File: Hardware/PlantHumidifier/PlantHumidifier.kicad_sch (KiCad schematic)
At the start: 10 parts

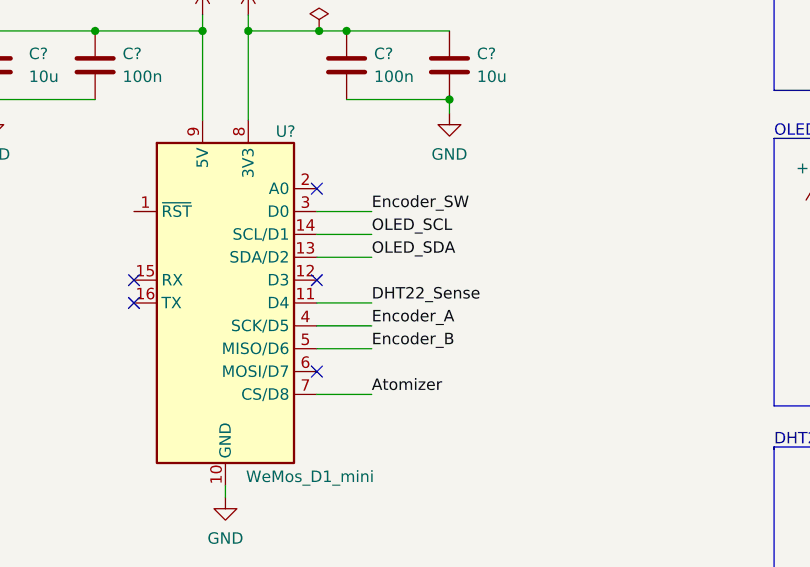
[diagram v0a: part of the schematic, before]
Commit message: Move DHT22 pin in code and schematic to D3 (GPIO 0); GPIO requires removal of DHT b/w resets
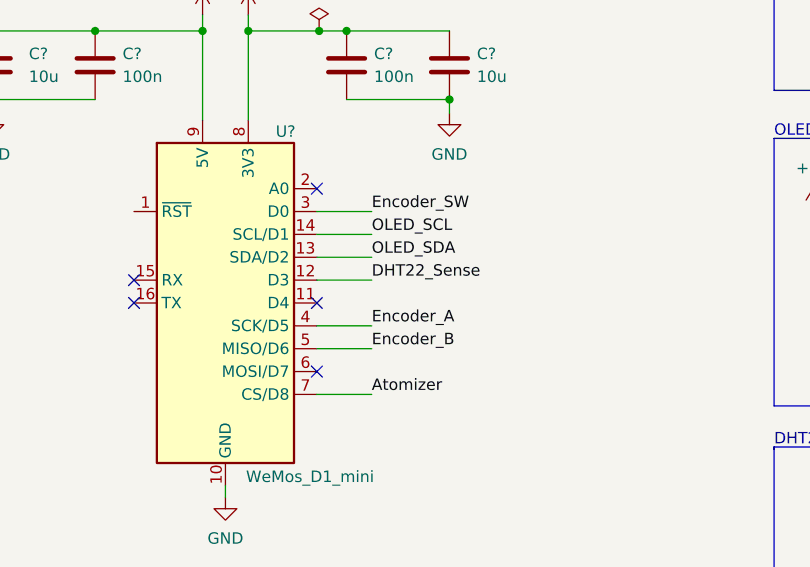
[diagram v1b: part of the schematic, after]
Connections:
- net DHT22_Sense: now also U?.12 (D3); no longer U?.11 (D4)
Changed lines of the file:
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@@
   (no_connect (at 125.476 116.078))
   (no_connect (at 105.156 105.918))
-  (no_connect (at 125.476 105.918))
+  (no_connect (at 125.476 108.458))
   (no_connect (at 105.156 108.458))
   (no_connect (at 125.476 95.758))
@@
     (stroke (width 0) (type default) (color 0 0 0 0))
   )
-  (wire (pts (xy 125.476 108.458) (xy 131.572 108.458))
+  (wire (pts (xy 125.476 105.918) (xy 131.572 105.918))
     (stroke (width 0) (type default) (color 0 0 0 0))
   )
@@
     (effects (font (size 1.27 1.27)) (justify left bottom))
   )
-  (label "DHT22_Sense" (at 131.572 108.458 0)
-    (effects (font (size 1.27 1.27)) (justify left bottom))
-  )
+  (label "DHT22_Sense" (at 131.572 105.918 0)
+    (effects (font (size 1.27 1.27)) (justify left bottom))
+  )

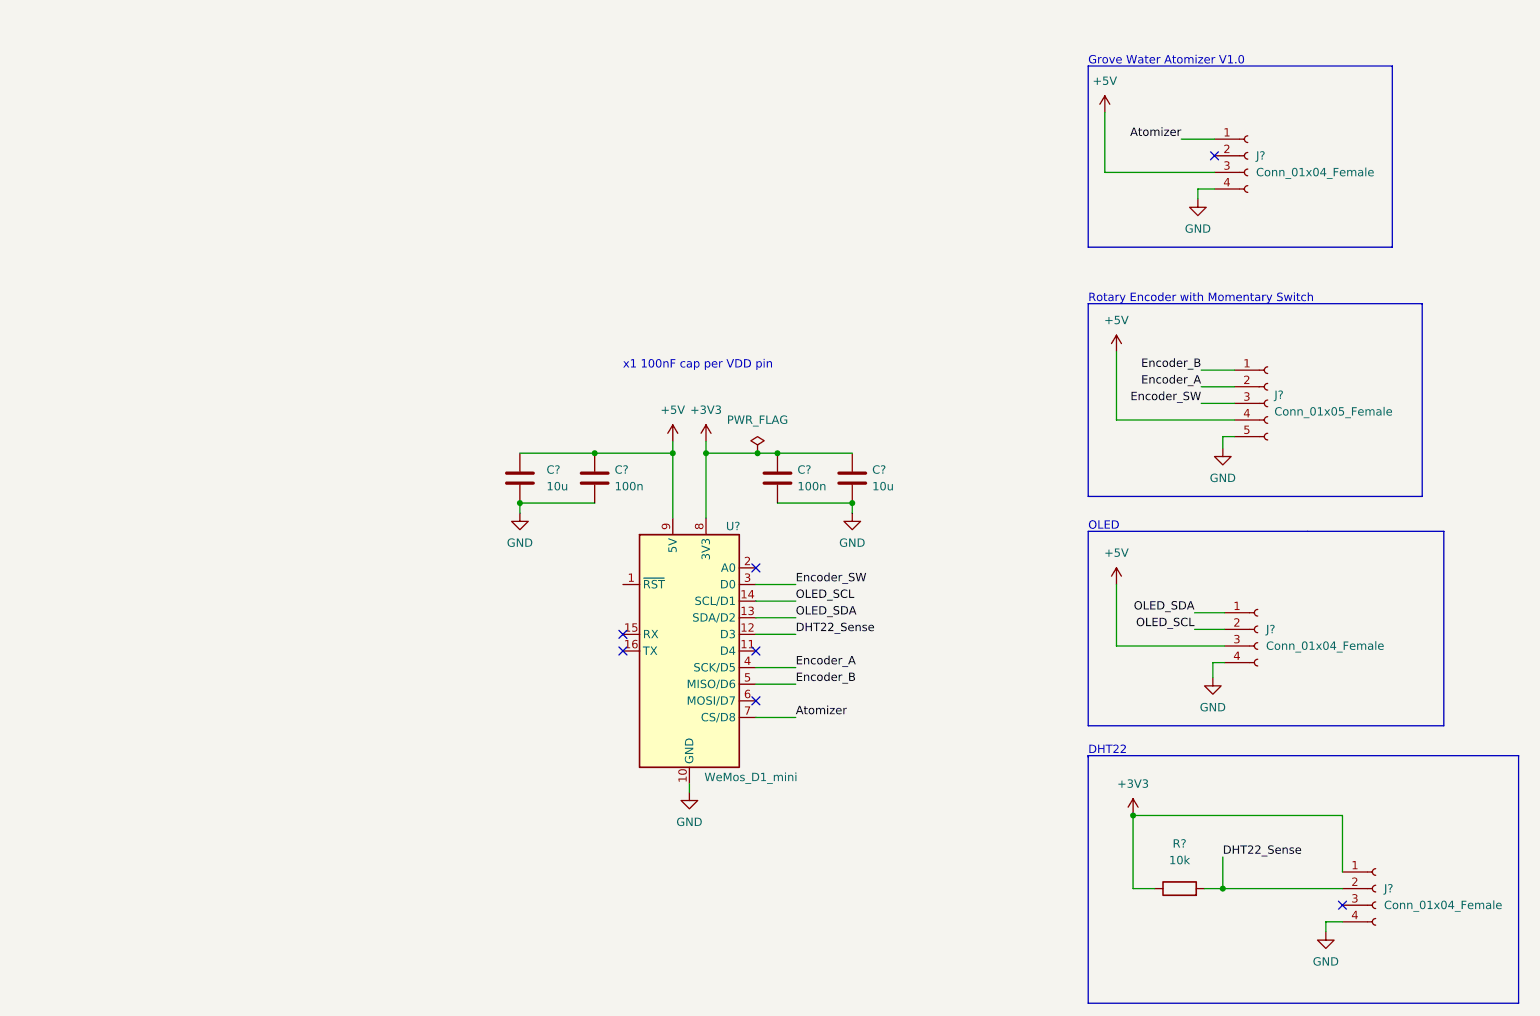
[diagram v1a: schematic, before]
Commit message: Schematic: Add an active low reset switch
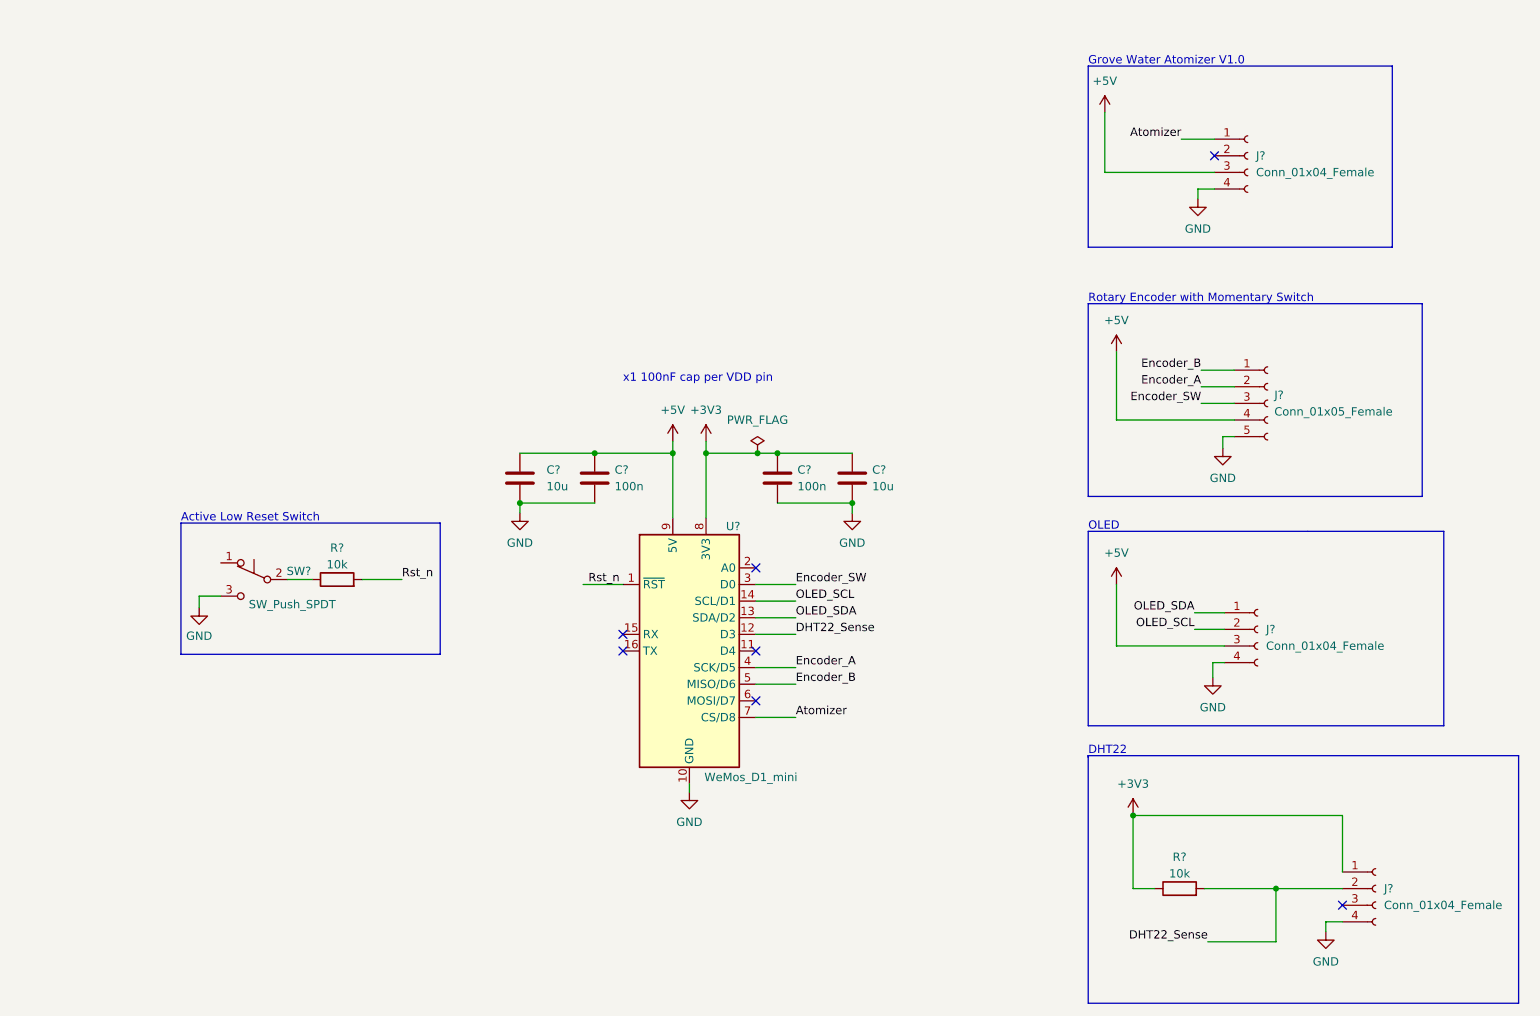
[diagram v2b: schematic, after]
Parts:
- added R?: 10k, symbol Device:R
- added SW?: SW_Push_SPDT, symbol Switch:SW_Push_SPDT
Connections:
- net GND: now also SW?.3 (C)
- net Rst_n: now reaches U?.1 (~{RST})
- net Rst_n: now also R?.2
- new net: R?.1, SW?.2 (B)
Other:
- note added: "Active Low Reset Switch"
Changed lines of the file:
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@@
   (junction (at 125.73 78.232) (diameter 0) (color 0 0 0 0)
   )
-  (junction (at 196.85 144.78) (diameter 0) (color 0 0 0 0)
-  )
   (junction (at 100.838 78.232) (diameter 0) (color 0 0 0 0)
   )
@@
   )
   (junction (at 112.776 78.232) (diameter 0) (color 0 0 0 0)
+  )
+  (junction (at 204.978 144.78) (diameter 0) (color 0 0 0 0)
   )
   (junction (at 128.778 78.232) (diameter 0) (color 0 0 0 0)
@@
     (stroke (width 0) (type default) (color 0 0 0 0))
   )
+  (polyline (pts (xy 77.216 108.966) (xy 37.592 108.966))
+    (stroke (width 0) (type default) (color 0 0 0 0))
+  )
   (wire (pts (xy 125.476 98.298) (xy 131.572 98.298))
     (stroke (width 0) (type default) (color 0 0 0 0))
@@
     (stroke (width 0) (type default) (color 0 0 0 0))
   )
+  (polyline (pts (xy 77.216 88.9) (xy 77.216 108.966))
+    (stroke (width 0) (type default) (color 0 0 0 0))
+  )
   (polyline (pts (xy 176.276 19.05) (xy 176.276 46.736))
     (stroke (width 0) (type default) (color 0 0 0 0))
@@
     (stroke (width 0) (type default) (color 0 0 0 0))
   )
-  (wire (pts (xy 196.85 144.78) (xy 215.138 144.78))
+  (polyline (pts (xy 37.592 88.9) (xy 77.216 88.9))
+    (stroke (width 0) (type default) (color 0 0 0 0))
+  )
+  (wire (pts (xy 194.056 144.78) (xy 204.978 144.78))
     (stroke (width 0) (type default) (color 0 0 0 0))
   )
@@
     (stroke (width 0) (type default) (color 0 0 0 0))
   )
+  (wire (pts (xy 204.978 144.78) (xy 204.978 152.908))
+    (stroke (width 0) (type default) (color 0 0 0 0))
+  )
   (polyline (pts (xy 222.758 46.736) (xy 222.758 19.05))
     (stroke (width 0) (type default) (color 0 0 0 0))
   )
+  (wire (pts (xy 194.564 152.908) (xy 204.978 152.908))
+    (stroke (width 0) (type default) (color 0 0 0 0))
+  )
   (wire (pts (xy 112.776 78.232) (xy 112.776 88.138))
     (stroke (width 0) (type default) (color 0 0 0 0))
@@
     (stroke (width 0) (type default) (color 0 0 0 0))
   )
-  (wire (pts (xy 194.056 144.78) (xy 196.85 144.78))
+  (wire (pts (xy 40.386 101.854) (xy 40.386 100.076))
     (stroke (width 0) (type default) (color 0 0 0 0))
   )
@@
     (stroke (width 0) (type default) (color 0 0 0 0))
   )
+  (wire (pts (xy 204.978 144.78) (xy 215.138 144.78))
+    (stroke (width 0) (type default) (color 0 0 0 0))
+  )
   (polyline (pts (xy 209.804 90.17) (xy 176.276 90.17))
     (stroke (width 0) (type default) (color 0 0 0 0))
@@
     (stroke (width 0) (type default) (color 0 0 0 0))
   )
+  (wire (pts (xy 40.386 100.076) (xy 43.688 100.076))
+    (stroke (width 0) (type default) (color 0 0 0 0))
+  )
   (wire (pts (xy 89.408 85.852) (xy 100.838 85.852))
     (stroke (width 0) (type default) (color 0 0 0 0))
   )
+  (wire (pts (xy 65.278 97.536) (xy 71.374 97.536))
+    (stroke (width 0) (type default) (color 0 0 0 0))
+  )
   (wire (pts (xy 128.778 78.232) (xy 140.208 78.232))
     (stroke (width 0) (type default) (color 0 0 0 0))
   )
+  (wire (pts (xy 53.848 97.536) (xy 57.658 97.536))
+    (stroke (width 0) (type default) (color 0 0 0 0))
+  )
   (polyline (pts (xy 176.276 119.888) (xy 230.632 119.888))
     (stroke (width 0) (type default) (color 0 0 0 0))
@@
     (stroke (width 0) (type default) (color 0 0 0 0))
   )
+  (polyline (pts (xy 37.592 108.966) (xy 37.592 88.9))
+    (stroke (width 0) (type default) (color 0 0 0 0))
+  )
   (wire (pts (xy 183.134 144.78) (xy 186.436 144.78))
     (stroke (width 0) (type default) (color 0 0 0 0))
   )
+  (wire (pts (xy 99.06 98.298) (xy 105.156 98.298))
+    (stroke (width 0) (type default) (color 0 0 0 0))
+  )
   (wire (pts (xy 196.85 77.47) (xy 196.85 75.692))
     (stroke (width 0) (type default) (color 0 0 0 0))
   )
-  (wire (pts (xy 196.85 139.954) (xy 196.85 144.78))
-    (stroke (width 0) (type default) (color 0 0 0 0))
-  )
   (polyline (pts (xy 176.276 55.372) (xy 176.276 84.836))
     (stroke (width 0) (type default) (color 0 0 0 0))
@@
     (stroke (width 0) (type default) (color 0 0 0 0))
   )
-  (text "x1 100nF cap per VDD pin" (at 105.156 65.532 0)
+  (text "x1 100nF cap per VDD pin" (at 105.156 67.564 0)
     (effects (font (size 1.27 1.27)) (justify left bottom))
   )
@@
     (effects (font (size 1.27 1.27)) (justify left bottom))
   )
+  (text "Active Low Reset Switch" (at 37.592 88.9 0)
+    (effects (font (size 1.27 1.27)) (justify left bottom))
+  )
   (label "OLED_SDA" (at 131.572 103.378 0)
     (effects (font (size 1.27 1.27)) (justify left bottom))
   )
   (label "DHT22_Sense" (at 131.572 105.918 0)
+    (effects (font (size 1.27 1.27)) (justify left bottom))
+  )
+  (label "Rst_n" (at 71.374 97.536 0)
     (effects (font (size 1.27 1.27)) (justify left bottom))
   )
@@
     (effects (font (size 1.27 1.27)) (justify right bottom))
   )
-  (label "DHT22_Sense" (at 196.85 139.954 0)
-    (effects (font (size 1.27 1.27)) (justify left bottom))
+  (label "Rst_n" (at 104.648 98.298 180)
+    (effects (font (size 1.27 1.27)) (justify right bottom))
+  )
+  (label "DHT22_Sense" (at 194.564 152.908 180)
+    (effects (font (size 1.27 1.27)) (justify right bottom))
   )
   (label "Atomizer" (at 190.5 30.226 180)
@@
     (pin "1")
   )
+  (symbol (lib_id "Switch:SW_Push_SPDT") (at 48.768 97.536 0) (mirror y) (unit 1)
+    (in_bom yes) (on_board yes)
+    (property "Reference" "SW?" (id 0) (at 55.626 96.266 0))
+    (property "Value" "SW_Push_SPDT" (id 1) (at 54.61 101.346 0))
+    (property "Footprint" "" (id 2) (at 48.768 97.536 0)
+      (effects (font (size 1.27 1.27)) hide)
+    )
+    (property "Datasheet" "~" (id 3) (at 48.768 97.536 0)
+      (effects (font (size 1.27 1.27)) hide)
+    )
+    (pin "1")
+    (pin "2")
+    (pin "3")
+  )
+  (symbol (lib_id "power:GND") (at 40.386 101.854 0) (unit 1)
+    (in_bom yes) (on_board yes)
+    (property "Reference" "#PWR?" (id 0) (at 40.386 108.204 0)
+      (effects (font (size 1.27 1.27)) hide)
+    )
+    (property "Value" "GND" (id 1) (at 40.386 106.172 0))
+    (property "Footprint" "" (id 2) (at 40.386 101.854 0)
+      (effects (font (size 1.27 1.27)) hide)
+    )
+    (property "Datasheet" "" (id 3) (at 40.386 101.854 0)
+      (effects (font (size 1.27 1.27)) hide)
+    )
+    (pin "1")
+  )
   (symbol (lib_id "Connector:Conn_01x04_Female") (at 202.184 105.156 0) (unit 1)
     (in_bom yes) (on_board yes) (fields_autoplaced)
@@
   )
   (symbol (lib_id "Device:R") (at 190.246 144.78 90) (unit 1)
-    (in_bom yes) (on_board yes) (fields_autoplaced)
-    (property "Reference" "R?" (id 0) (at 190.246 137.922 90))
-    (property "Value" "10k" (id 1) (at 190.246 140.462 90))
+    (in_bom yes) (on_board yes)
+    (property "Reference" "R?" (id 0) (at 190.246 139.954 90))
+    (property "Value" "10k" (id 1) (at 190.246 142.494 90))
     (property "Footprint" "" (id 2) (at 190.246 146.558 90)
       (effects (font (size 1.27 1.27)) hide)
@@
     )
     (property "Datasheet" "~" (id 3) (at 89.408 82.042 0)
+      (effects (font (size 1.27 1.27)) hide)
+    )
+    (pin "1")
+    (pin "2")
+  )
+  (symbol (lib_id "Device:R") (at 61.468 97.536 90) (unit 1)
+    (in_bom yes) (on_board yes)
+    (property "Reference" "R?" (id 0) (at 61.468 92.71 90))
+    (property "Value" "10k" (id 1) (at 61.468 95.25 90))
+    (property "Footprint" "" (id 2) (at 61.468 99.314 90)
+      (effects (font (size 1.27 1.27)) hide)
+    )
+    (property "Datasheet" "~" (id 3) (at 61.468 97.536 0)
       (effects (font (size 1.27 1.27)) hide)
     )
@@
       (reference "#PWR?") (unit 1) (value "+5V") (footprint "")
     )
+    (path "/7516ccb2-eea9-42e0-b154-48428b1c1de8"
+      (reference "#PWR?") (unit 1) (value "GND") (footprint "")
+    )
     (path "/8848dd79-718c-4217-9cb5-0c12188193bc"
       (reference "#PWR?") (unit 1) (value "+5V") (footprint "")
@@
       (reference "R?") (unit 1) (value "10k") (footprint "")
     )
+    (path "/e7e820f3-59b8-44fe-b769-6d65c3132a62"
+      (reference "R?") (unit 1) (value "10k") (footprint "")
+    )
+    (path "/68aa1fe7-b13a-4afc-9183-41cdcae6d437"
+      (reference "SW?") (unit 1) (value "SW_Push_SPDT") (footprint "")
+    )
     (path "/fb8daade-f4cb-4b21-85db-6e6f772ccb5f"

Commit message: Schematic: Add page Title + Info
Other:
- title: (none) -> Plant Humidifier
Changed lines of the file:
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@@
 (kicad_sch (version 20211123) (generator eeschema)
   (paper "A4")
+  (title_block
+    (title "Plant Humidifier")
+    (date "2023-01-11")
+    (rev "A")
+    (comment 1 "Michael Ly")
+    (comment 2 "Github.com/Michael-Q-Ly")
+  )
   (junction (at 117.856 78.232) (diameter 0) (color 0 0 0 0)
   )
